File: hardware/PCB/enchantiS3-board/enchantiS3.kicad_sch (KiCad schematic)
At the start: 73 parts, among them J1 USB_C_Receptacle_USB2.0, Q1 BSS138, Q2 BSS138, Q3 BSS138, SW1 B3U-1000P, SW2 B3U-1000P, U1 USBLC6-2P6, U2 MCP73871, U3 NCP167AMX330TBG, U4 NCP167AMX180TBG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

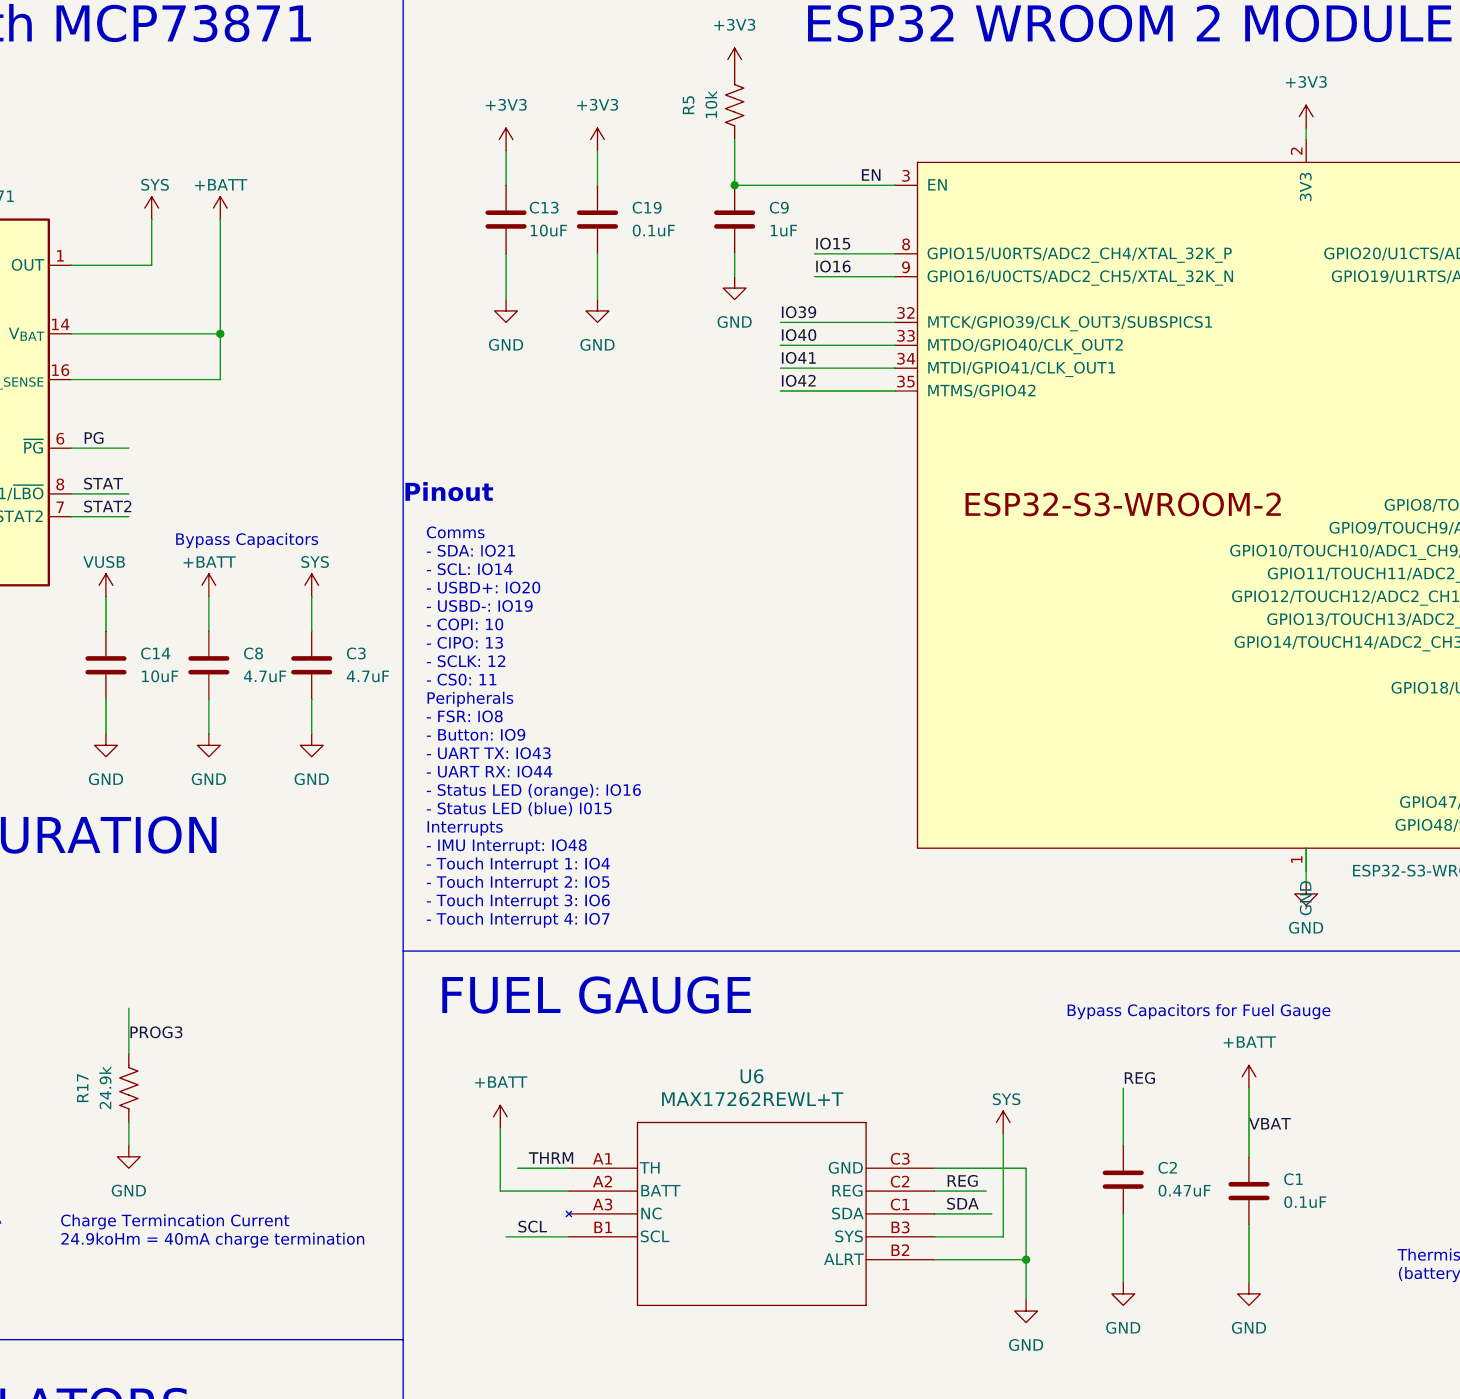
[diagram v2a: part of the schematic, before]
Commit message: fixed wrong connection between fuel gauge and system load
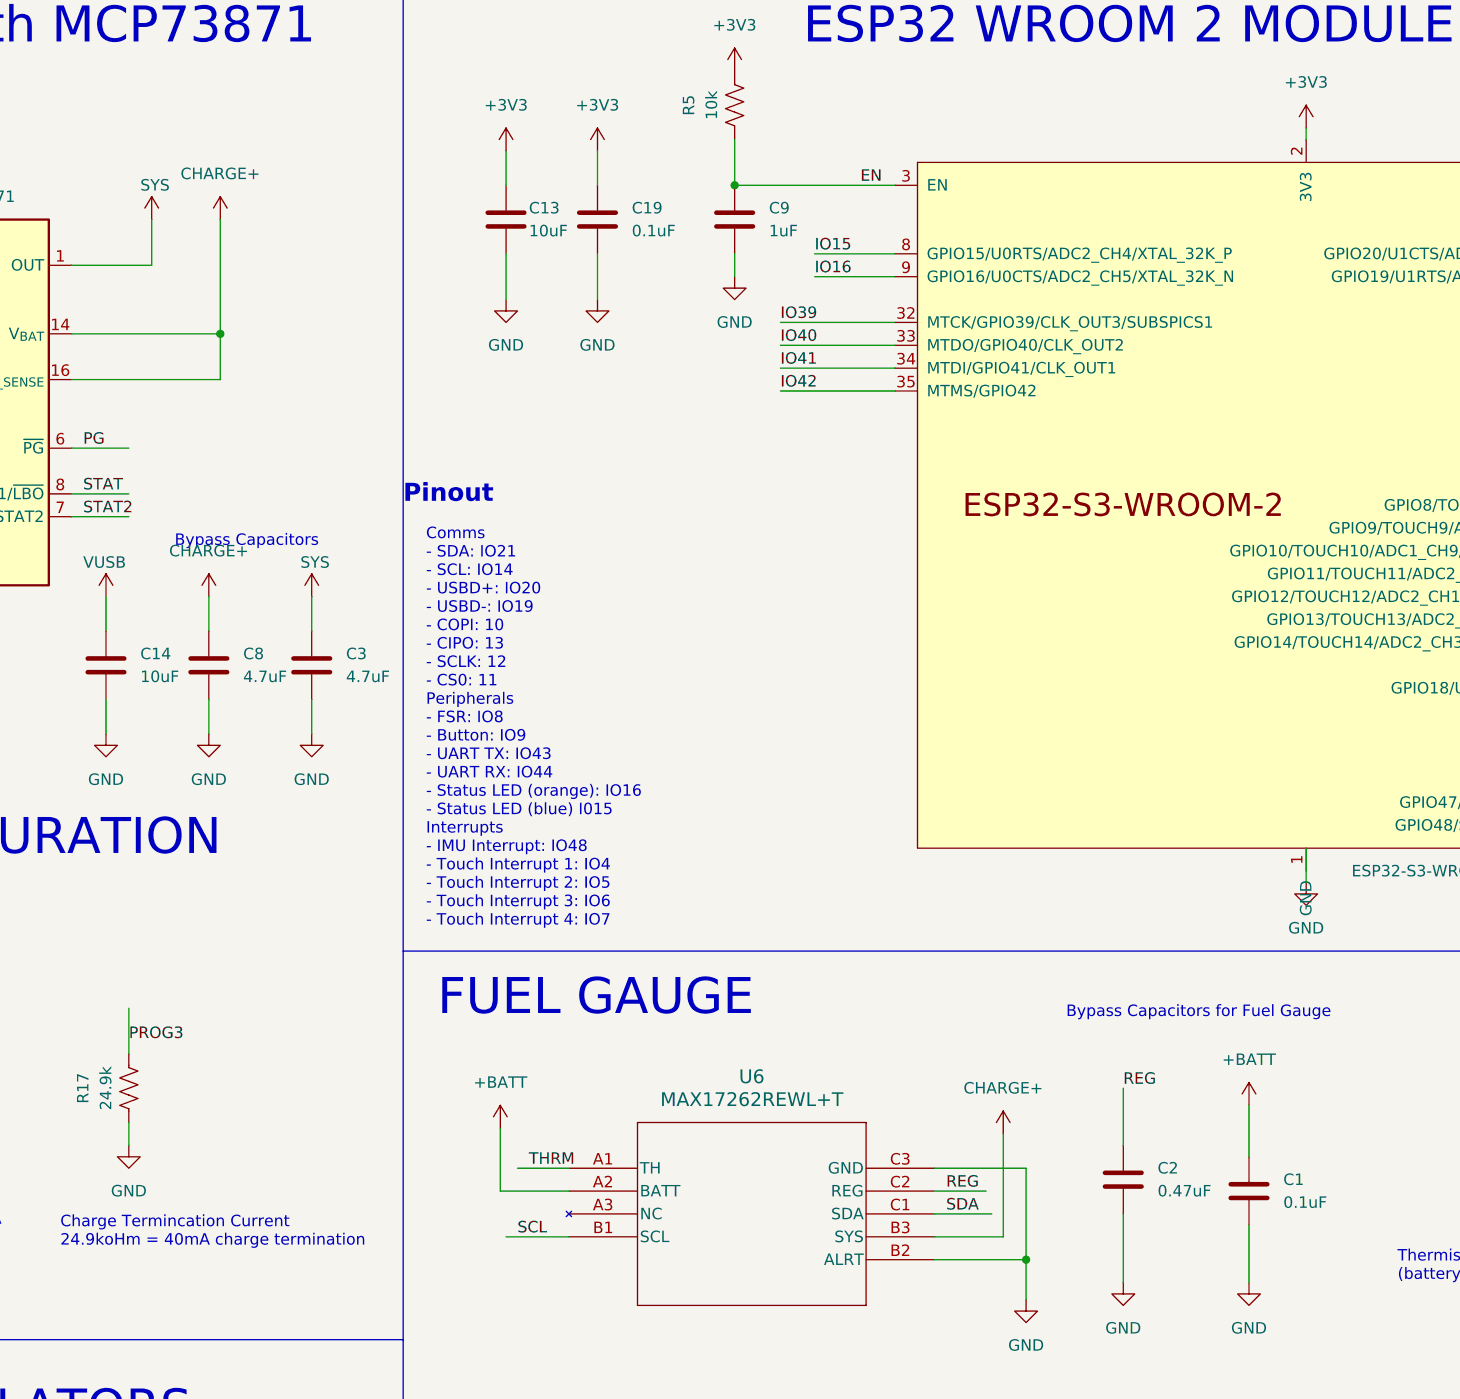
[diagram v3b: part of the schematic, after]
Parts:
- removed SYS7: SYS, symbol power-symbols:VSYS
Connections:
- net +BATT: no longer C8.1, U2.14 (V_{BAT}), U2.15 (V_{BAT}), U2.16 (V_{BAT_SENSE})
- net SYS: no longer U6.B3 (SYS)
- new net CHRG+: C8.1, U2.14 (V_{BAT}), U2.15 (V_{BAT}), U2.16 (V_{BAT_SENSE}), U6.B3 (SYS)
